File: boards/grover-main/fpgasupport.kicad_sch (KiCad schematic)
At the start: 49 parts

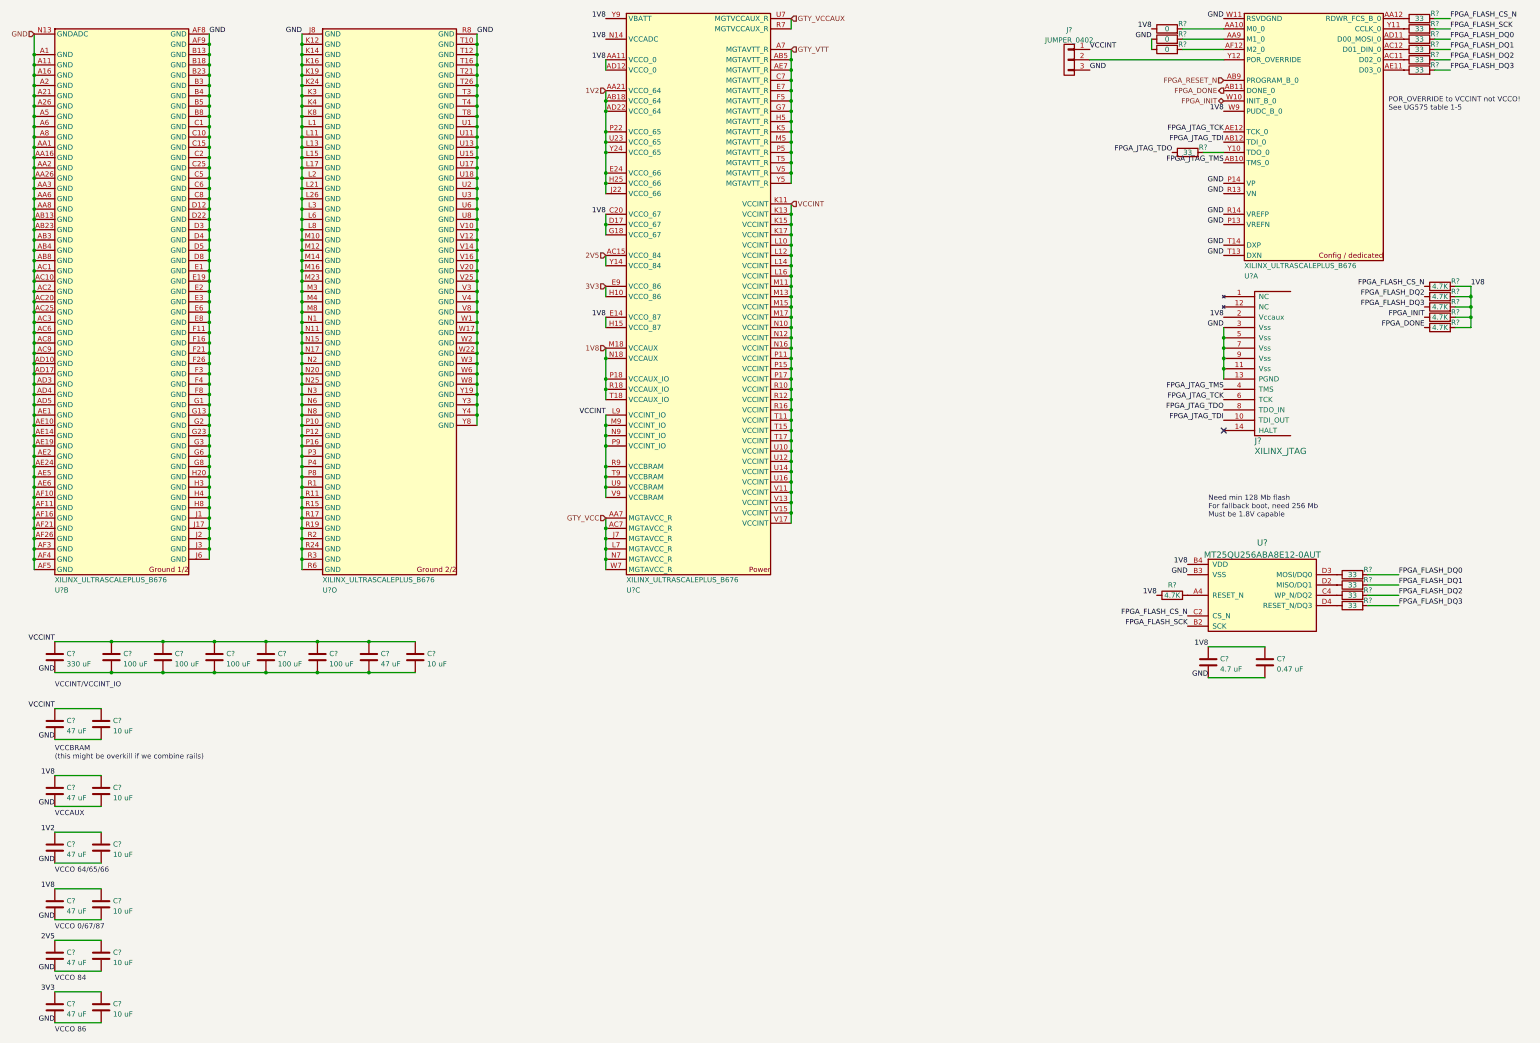
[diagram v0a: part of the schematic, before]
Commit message: Continued initial schematic capture
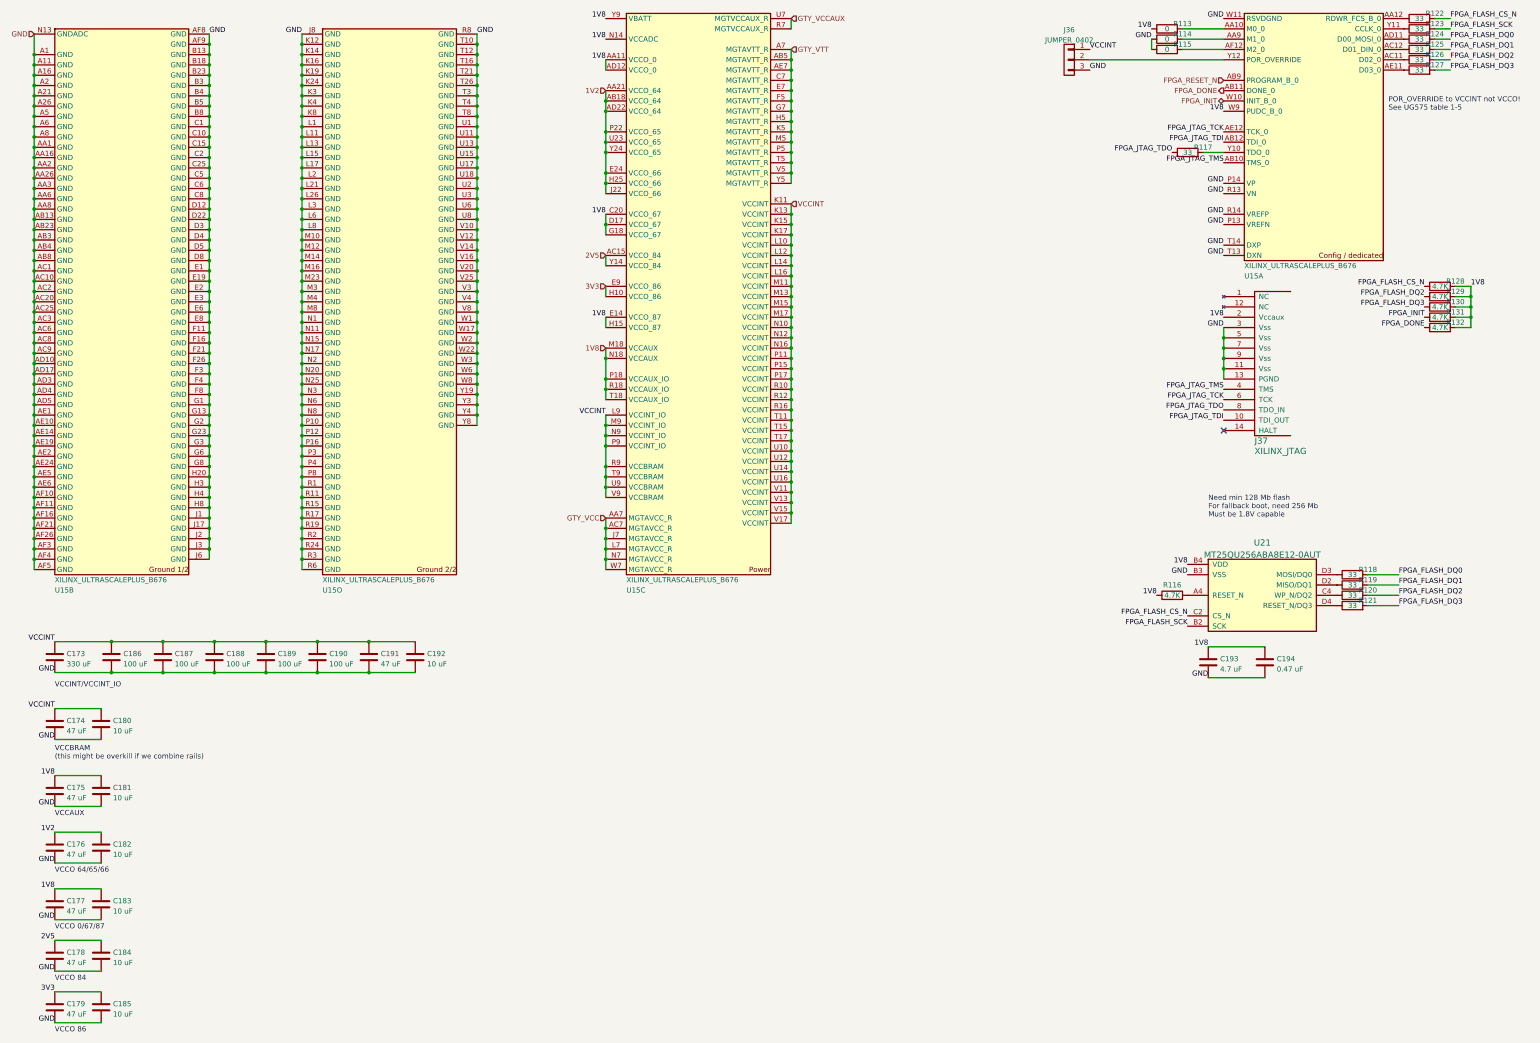
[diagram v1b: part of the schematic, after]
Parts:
- gave numbers to parts that had none: 46
